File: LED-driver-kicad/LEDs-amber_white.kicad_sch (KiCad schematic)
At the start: 53 parts, among them Q4 Q_NMOS_GDS, Q5 Q_NMOS_GDS, Q6 Q_NMOS_GDS, U11 74AHC1G14, U7 MIC3205YML-TR

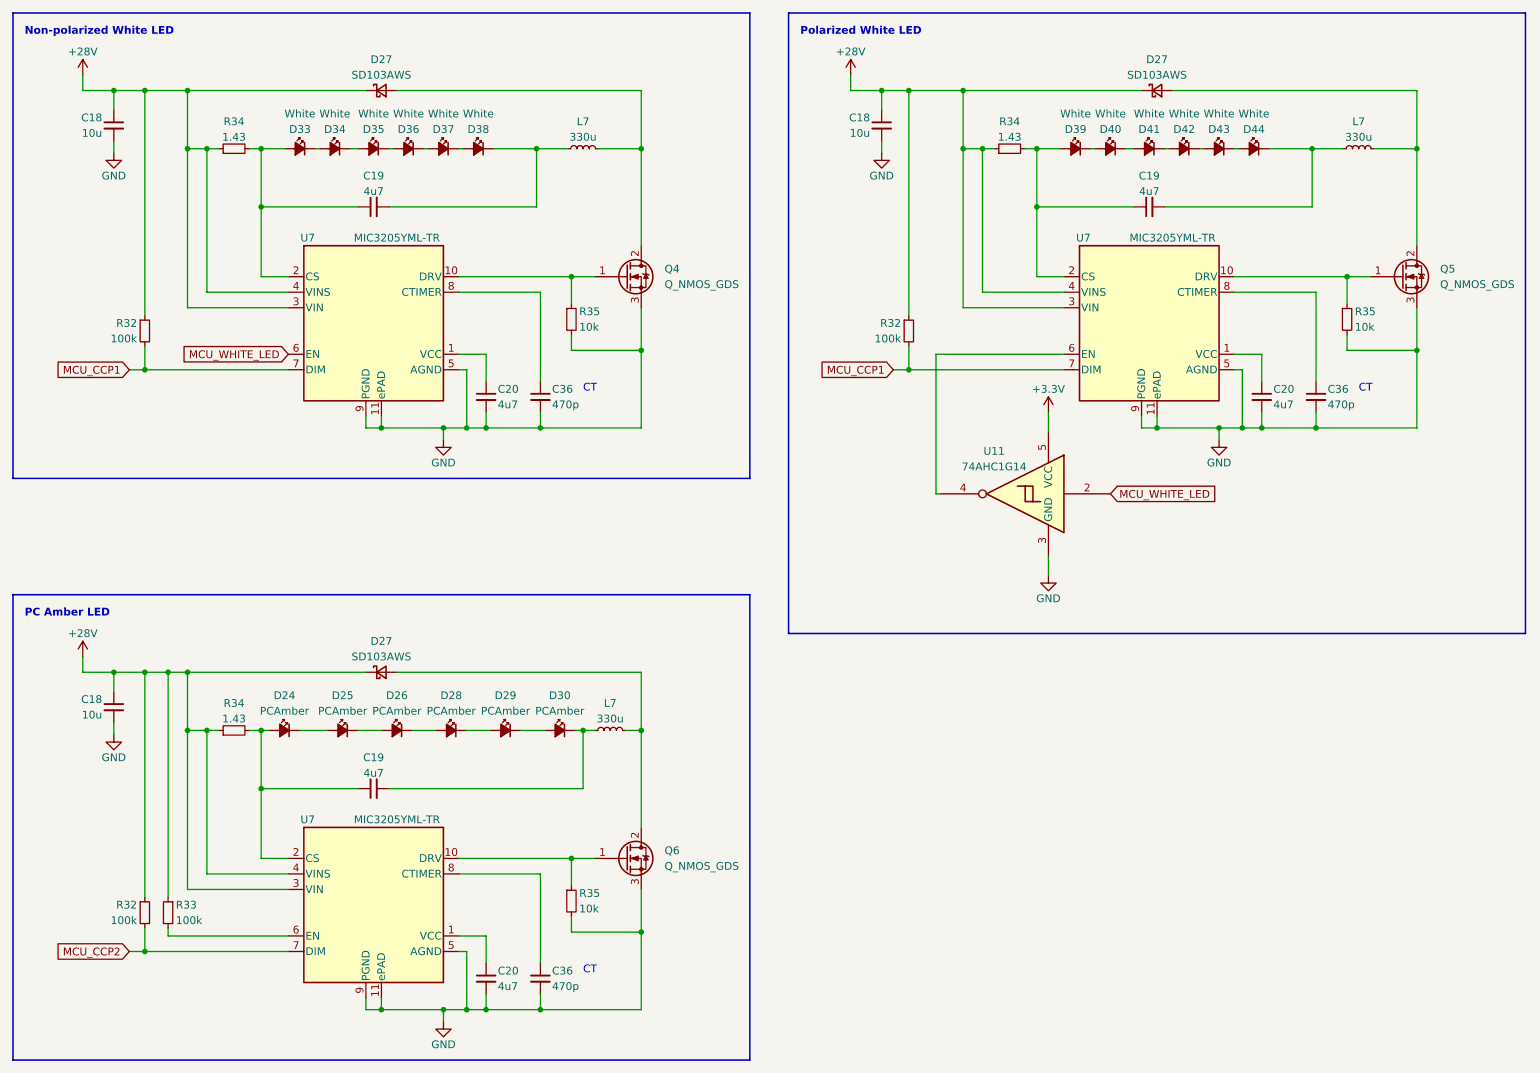
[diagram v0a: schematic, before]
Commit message: add test points, net ties to schematics
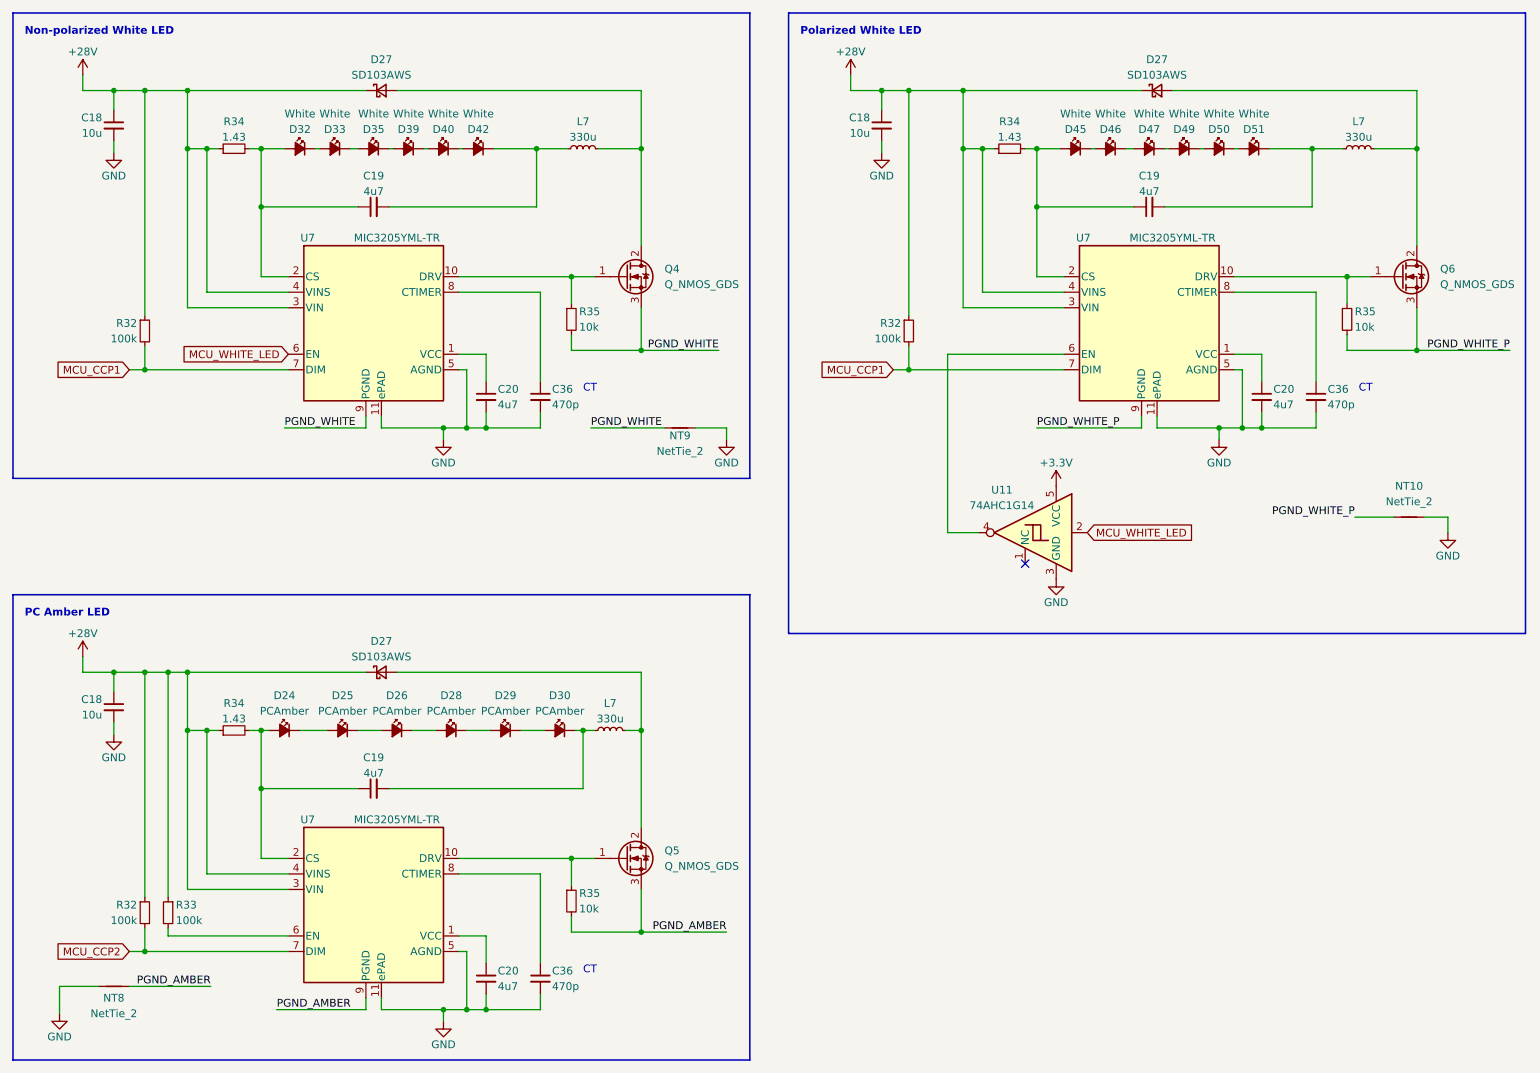
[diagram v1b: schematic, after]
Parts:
- added NT10, NT8, NT9: NetTie_2, NetTie:NetTie-2_SMD_Pad0.5mm, symbol Device:NetTie_2
- renumbered D33 to D32, D34 to D33, D36 to D39, D37 to D40, D38 to D42, D39 to D45, D40 to D46, D41 to D47, D42 to D49, D43 to D50, D44 to D51, Q6 to Q5, Q5 to Q6
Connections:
- net GND: now also NT10.2, NT8.1, NT9.2; no longer Q4.3 (S), Q5.3 (S), Q6.3 (S), R35.2, R35.2, R35.2, U7.9 (PGND), U7.9 (PGND), U7.9 (PGND)
- new net PGND_AMBER: NT8.2, Q5.3 (S), R35.2, U7.9 (PGND)
- new net PGND_WHITE: NT9.1, Q4.3 (S), R35.2, U7.9 (PGND)
- new net PGND_WHITE_P: NT10.1, Q6.3 (S), R35.2, U7.9 (PGND)
- no-connect marks 0 -> 1
